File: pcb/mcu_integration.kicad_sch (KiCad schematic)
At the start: 26 parts, among them J1 Micro_SD_Card, J3 Conn_01x06, U1 STM32F103RBTx, Y1 ECS-80-18-5PX-GM-TR

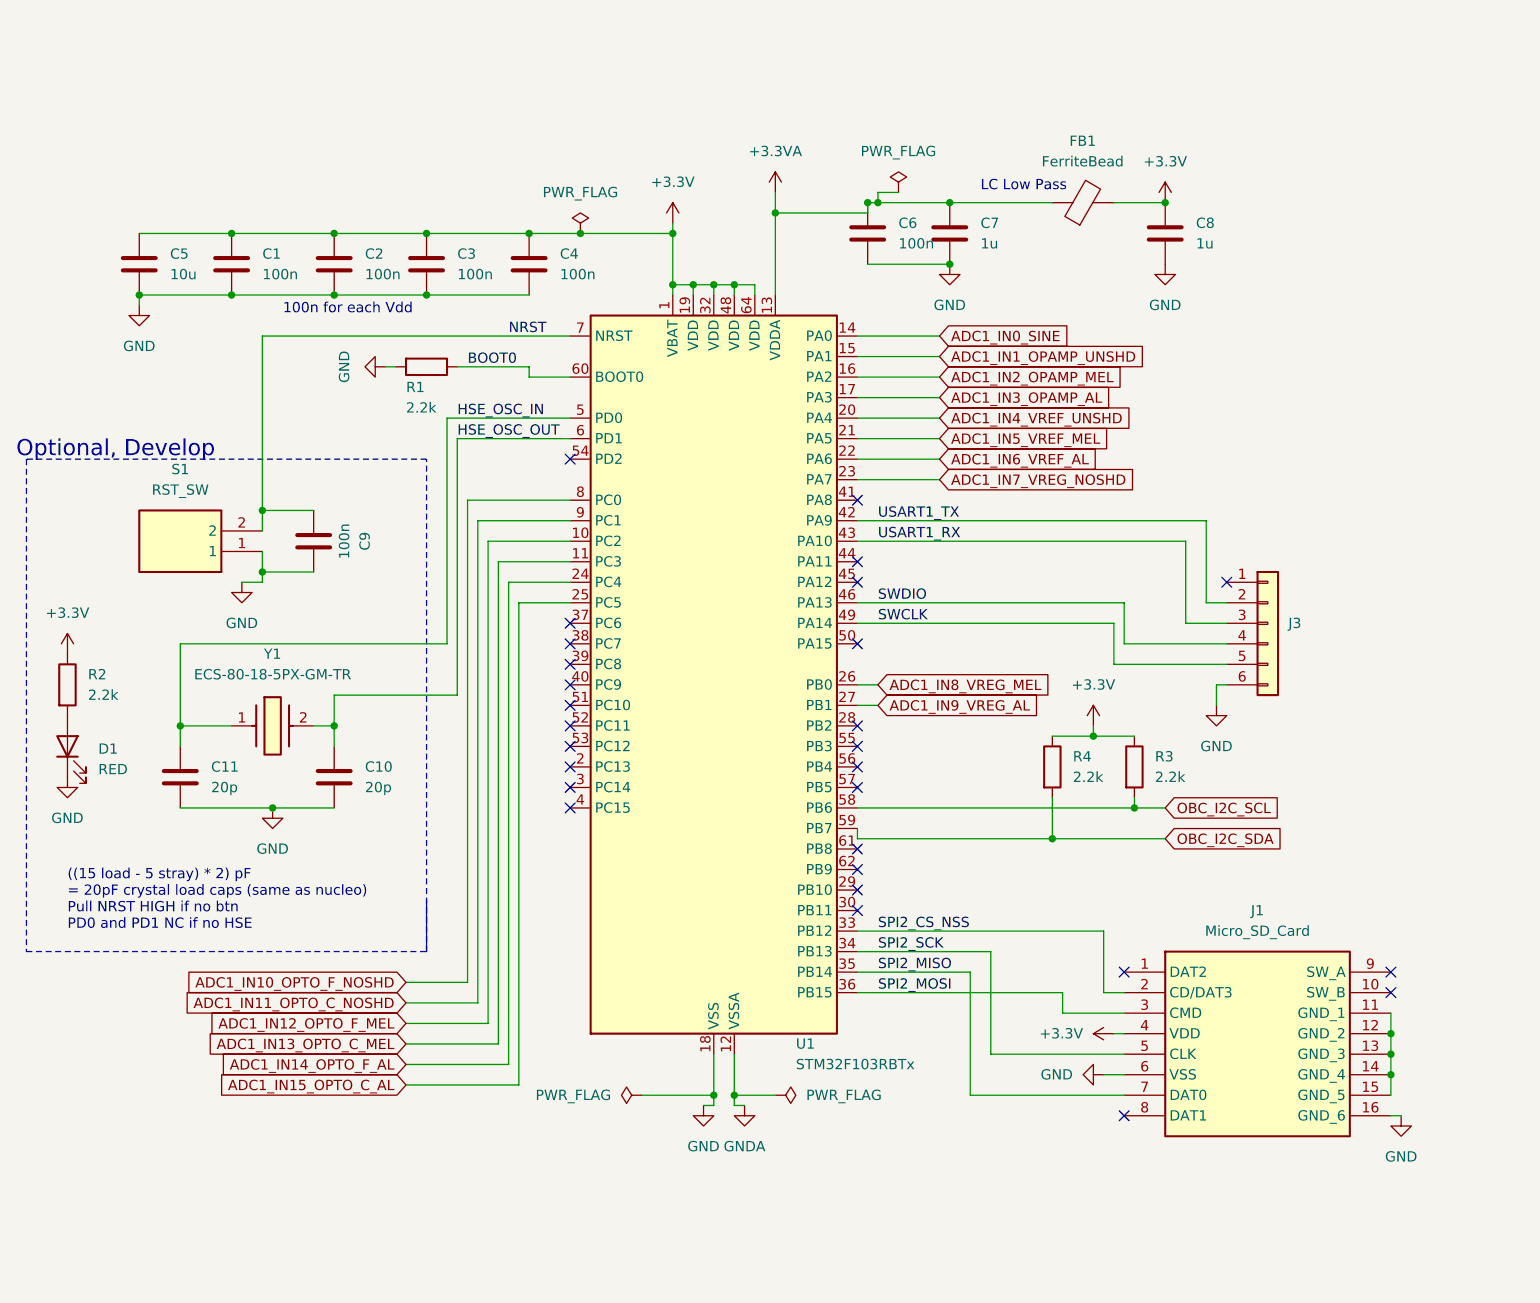
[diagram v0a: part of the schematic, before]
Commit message: First Major PCB layout and routing (#10)
* first bulk commit of routing

* removed about 300 pcb ERC warnings

* removed all pcb DRC errors/warnings

* silkscreen: remove part num from inside part, cleanup

* add silk labels for each pin, my final cleanup

* remove all errors and suppress unspecified connections warnings in schematic ERC

---------

Co-authored-by: evanc2987 <evan.campbell2987@gmail.com>
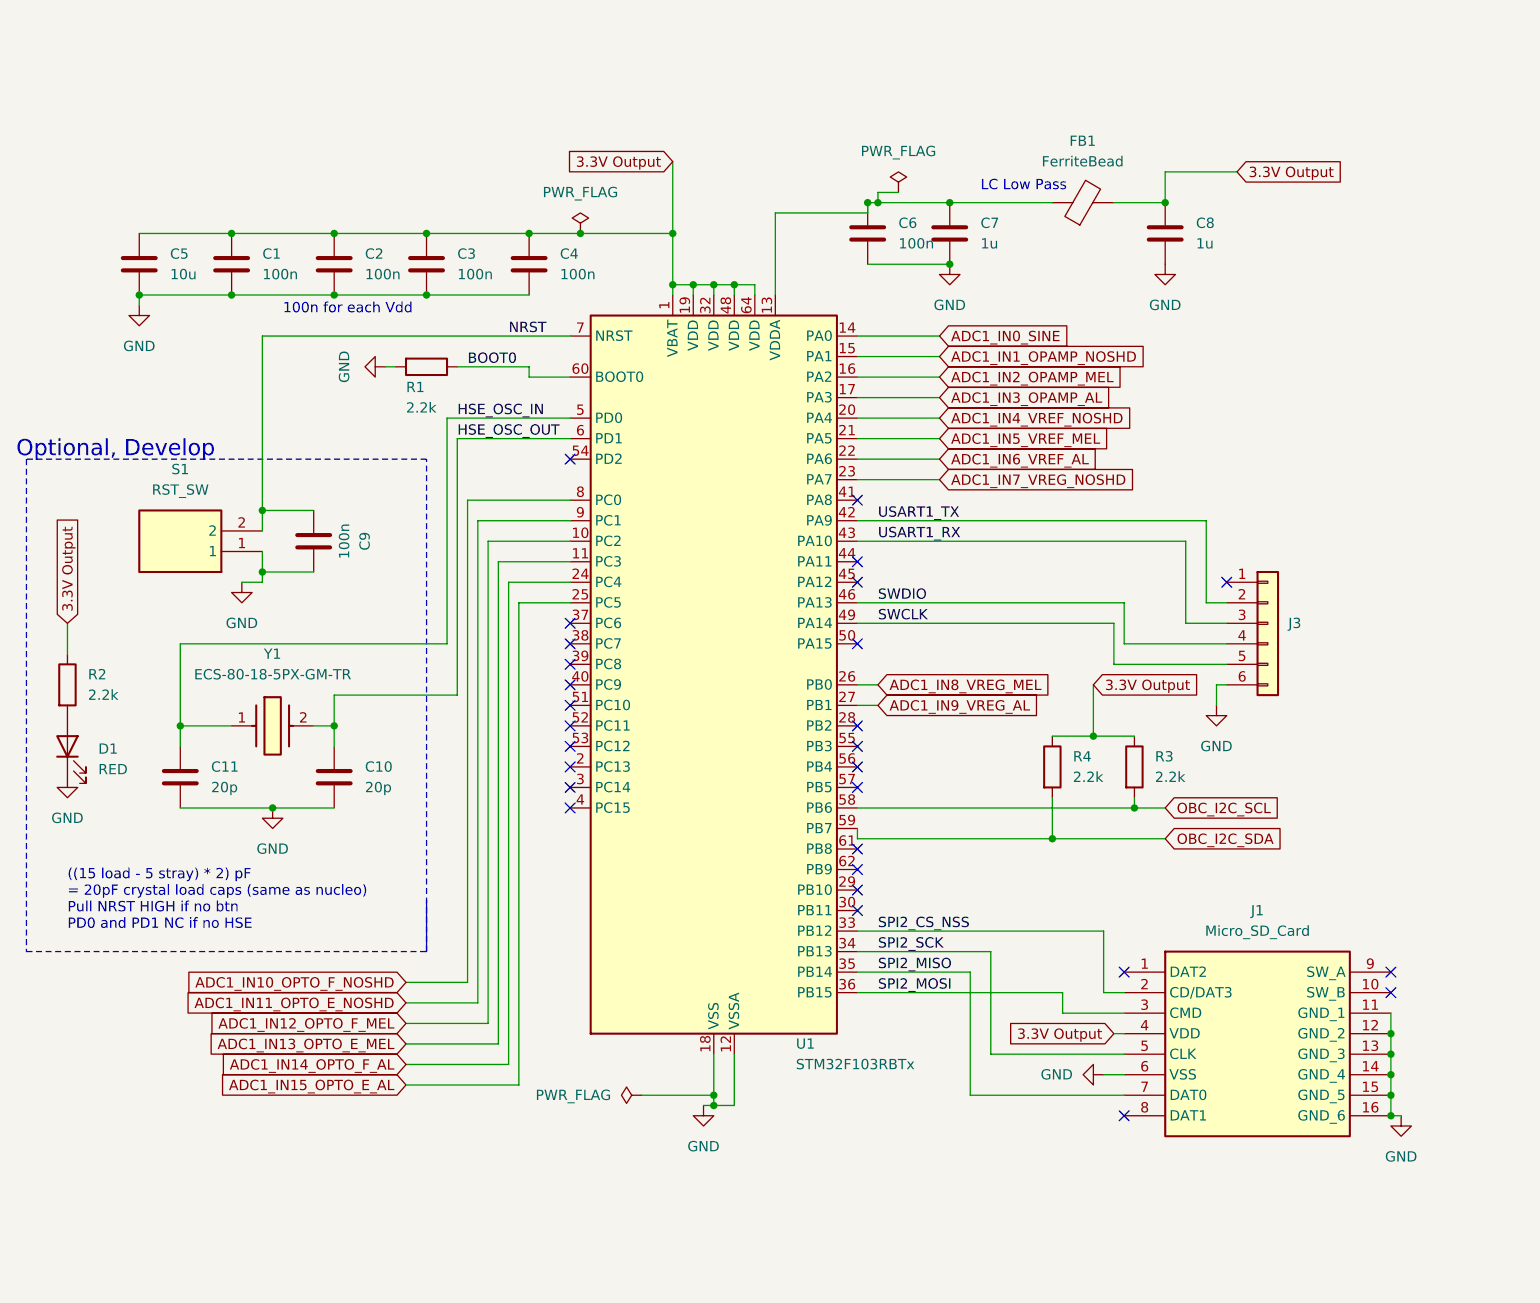
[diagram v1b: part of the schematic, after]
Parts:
- J1: footprint 22017781 -> (none)
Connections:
- net GNDA is gone; now on net GND: U1.12 (VSSA)
- net GND: now also J1.11 (GND_1), J1.12 (GND_2), J1.13 (GND_3), J1.14 (GND_4), J1.15 (GND_5)
- net +3.3V renamed 3.3V Output
- net +3.3VA: no longer names the net of C6.1, C7.1, FB1.1, U1.13 (VDDA)
- net ADC1_IN11_OPTO_C_NOSHD renamed ADC1_IN11_OPTO_E_NOSHD
- net ADC1_IN13_OPTO_C_MEL renamed ADC1_IN13_OPTO_E_MEL
- net ADC1_IN15_OPTO_C_AL renamed ADC1_IN15_OPTO_E_AL
- net ADC1_IN1_OPAMP_UNSHD renamed ADC1_IN1_OPAMP_NOSHD
- net ADC1_IN4_VREF_UNSHD renamed ADC1_IN4_VREF_NOSHD
